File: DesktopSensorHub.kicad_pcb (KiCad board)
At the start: 2 copper layers, 44 parts, among them J1 USB_C_Receptacle_USB2.0, SW1 TS02-66-50-BK-160-LCR-D, U1 RP2040, U2 APDS-9960, U3 AP2112K-3.3, U5 W25Q32JVSS, Y1 12 MHZ

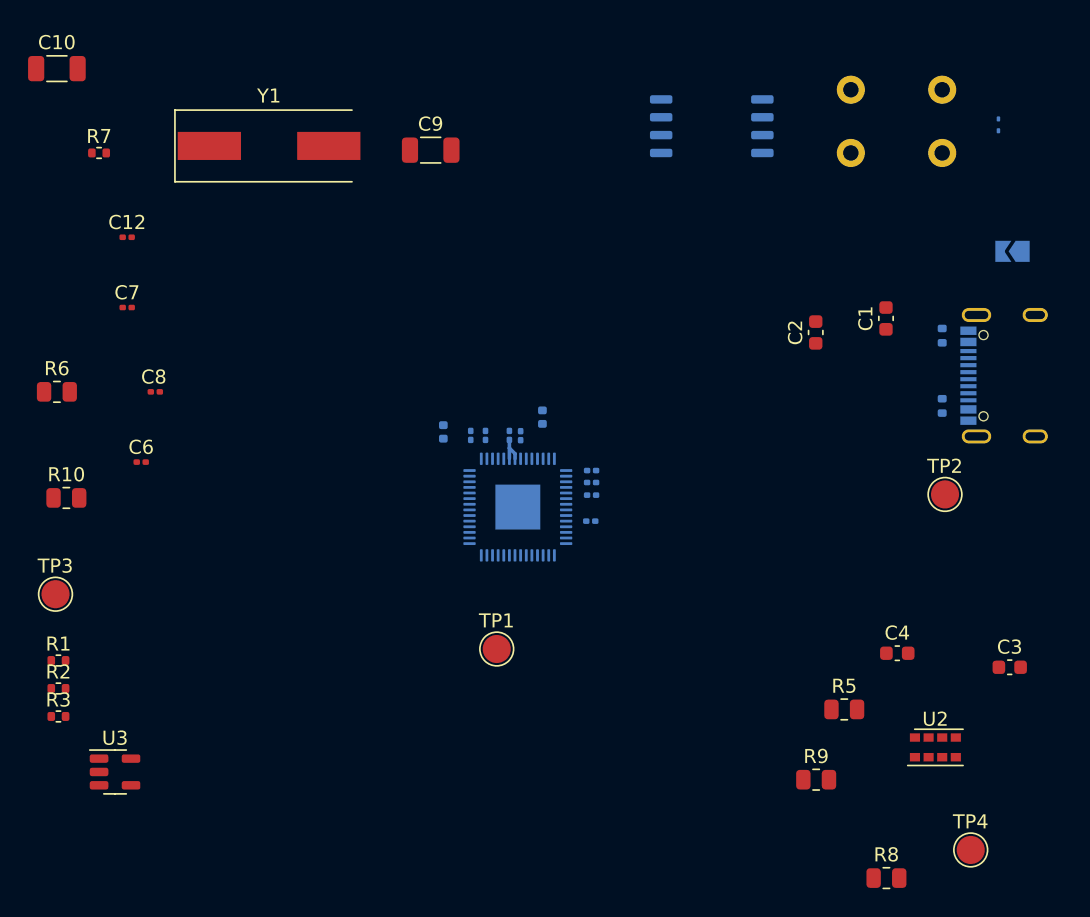
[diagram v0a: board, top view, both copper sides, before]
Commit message: finish layout, include design files sent to OSHPark
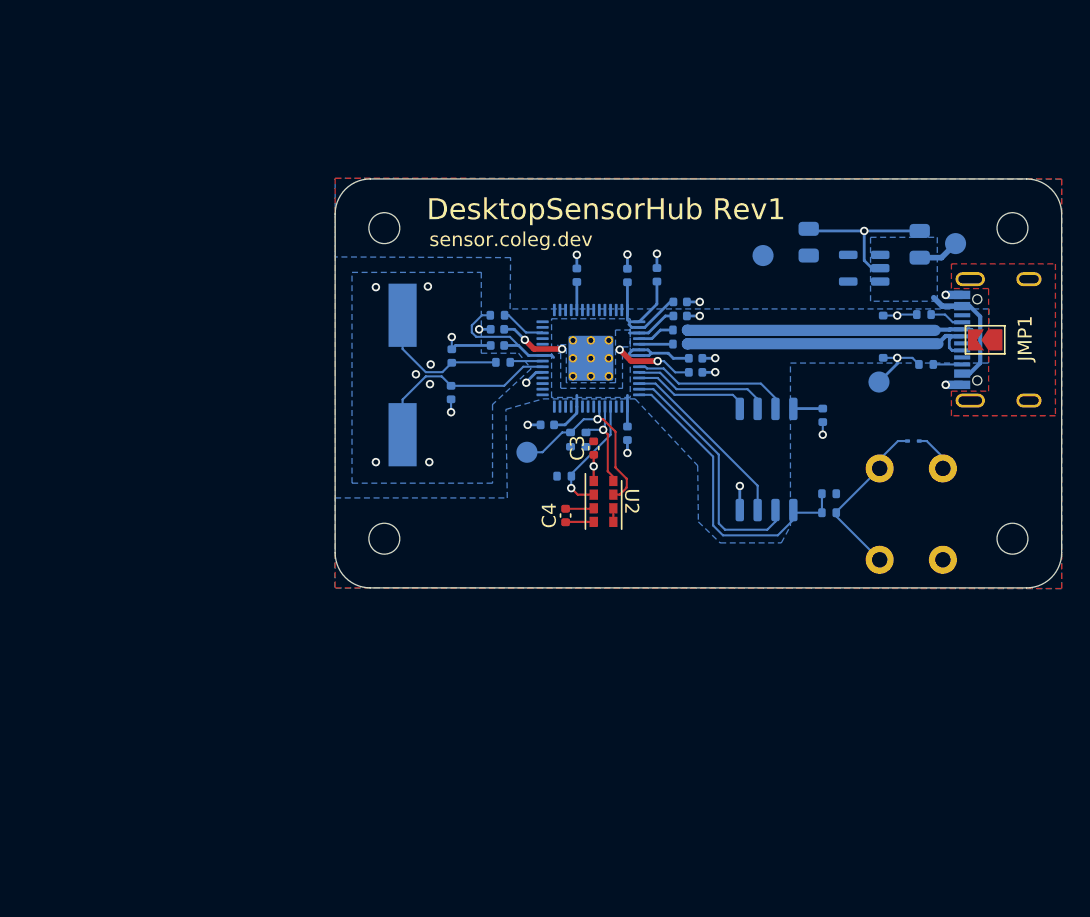
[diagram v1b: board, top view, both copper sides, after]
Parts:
- added REF**: MountingHole_2.2mm_M2, MountingHole:MountingHole_2.2mm_M2, F.Cu at (98.3, 88.5)
- added REF**: MountingHole_2.2mm_M2, MountingHole:MountingHole_2.2mm_M2, F.Cu at (143.0, 88.5)
- added REF**: MountingHole_2.2mm_M2, MountingHole:MountingHole_2.2mm_M2, F.Cu at (143.0, 66.3)
- added REF**: MountingHole_2.2mm_M2, MountingHole:MountingHole_2.2mm_M2, F.Cu at (98.3, 66.3)
- C1, C2: footprint Capacitor_SMD:C_0603_1608Metric -> Capacitor_SMD:C_0402_1005Metric; moved to B.Cu
- C10, C9: footprint Capacitor_SMD:C_1206_3216Metric -> Capacitor_SMD:C_0402_1005Metric; moved to B.Cu
- C12, C8: footprint Capacitor_SMD:C_0201_0603Metric -> Capacitor_SMD:C_0402_1005Metric; moved to B.Cu
- C13, C14, C15, C16, C17, C18, C19, C20: footprint Capacitor_SMD:C_0201_0603Metric -> Capacitor_SMD:C_0402_1005Metric
- C3, C4: footprint Capacitor_SMD:C_0603_1608Metric -> Capacitor_SMD:C_0402_1005Metric
- C6, C7: footprint Capacitor_SMD:C_0201_0603Metric -> Capacitor_SMD:C_0805_2012Metric; moved to B.Cu
- JMP1: moved to F.Cu
- R1, R2, R3, R7, U3, Y1: moved to B.Cu
- R10, R5, R6, R8, R9: footprint Resistor_SMD:R_0805_2012Metric -> Resistor_SMD:R_0402_1005Metric; moved to B.Cu
- TP1, TP2, TP3, TP4: footprint TestPoint:TestPoint_Pad_D2.0mm -> TestPoint:TestPoint_Pad_D1.5mm; moved to B.Cu
- U1: footprint Package_DFN_QFN:QFN-56-1EP_7x7mm_P0.4mm_EP3.2x3.2mm -> DesktopSensorHub footprints:RP2040-QFN-56
- moved TP3 68.7 mm to (138.9, 67.5), turned to 180 degrees
- moved U3 64.2 mm to (132.4, 69.2), turned to 180 degrees
- moved C6 57.5 mm to (136.4, 67.5), turned to 90 degrees
- moved R1 55.8 mm to (129.9, 86.6)
- moved R10 54.3 mm to (129.9, 85.2), turned to 180 degrees
- moved R3 51.6 mm to (119.3, 74.6), turned to 180 degrees
- moved R2 51.1 mm to (119.3, 73.6), turned to 180 degrees
- moved C7 48.7 mm to (128.5, 67.3), turned to 90 degrees
- moved C8 47.5 mm to (129.5, 79.7), turned to -90 degrees
- moved TP4 42.4 mm to (108.5, 82.3), turned to 180 degrees
- moved C12 41.6 mm to (120.5, 76.6)
- moved R8 37.8 mm to (112.7, 81.4), turned to 90 degrees
- moved C10 34.8 mm to (103.1, 75.5), turned to -90 degrees
- moved TP1 33.8 mm to (125.2, 68.3), turned to 180 degrees
- moved C3 33.5 mm to (113.2, 82.0), turned to 90 degrees
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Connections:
- C1 pad 1: Net-(C1-Pad1) -> /USB_D-
- C14 pad 1: +3.3V -> +3V3
- C15 pad 1: +3.3V -> +3V3
- C16 pad 1: +3.3V -> +3V3
- C17 pad 1: +3.3V -> +3V3
- C18 pad 1: +3.3V -> +3V3
- C19 pad 1: +3.3V -> +3V3
- C2 pad 1: Net-(C2-Pad1) -> /USB_D+
- C20 pad 1: +3.3V -> +3V3
- C21 pad 1: +3.3V -> +3V3
- J1 pad A6: Net-(C2-Pad1) -> /USB_D+
- J1 pad A7: Net-(C1-Pad1) -> /USB_D-
- J1 pad B6: Net-(C2-Pad1) -> /USB_D+
- J1 pad B7: Net-(C1-Pad1) -> /USB_D-
- R2 pad 1: Net-(C1-Pad1) -> /USB_D-
- R2 pad 2: /USB_D- -> Net-(U1-USB_DM)
- R3 pad 1: Net-(C2-Pad1) -> /USB_D+
- R3 pad 2: /USB_D+ -> Net-(U1-USB_DP)
- R5 pad 2: Net-(U1-GPIO18) -> Net-(U1-GPIO4)
- R8 pad 2: Net-(U1-GPIO17) -> Net-(U1-GPIO3)
- R9 pad 2: Net-(U1-GPIO16) -> Net-(U1-GPIO2)
- TP1 pad 1: Net-(U1-RUN) -> +3V3
- TP3 pad 1: Net-(D1-A1) -> Net-(U3-EN)
- TP4 pad 1: Net-(U1-GPIO18) -> Net-(U1-GPIO4)
- U1 pad 1: +3.3V -> +3V3
- U1 pad 10: +3.3V -> +3V3
- U1 pad 22: +3.3V -> +3V3
- U1 pad 27: Net-(U1-GPIO16) -> unconnected-(U1-GPIO16-Pad27)
- U1 pad 28: Net-(U1-GPIO17) -> unconnected-(U1-GPIO17-Pad28)
- U1 pad 29: Net-(U1-GPIO18) -> unconnected-(U1-GPIO18-Pad29)
- U1 pad 33: +3.3V -> +3V3
- U1 pad 4: unconnected-(U1-GPIO2-Pad4) -> Net-(U1-GPIO2)
- U1 pad 42: +3.3V -> +3V3
- U1 pad 43: +3.3V -> +3V3
- U1 pad 44: +3.3V -> +3V3
- U1 pad 46: /USB_D- -> Net-(U1-USB_DM)
- U1 pad 47: /USB_D+ -> Net-(U1-USB_DP)
- U1 pad 48: +3.3V -> +3V3
- U1 pad 49: +3.3V -> +3V3
- U1 pad 5: unconnected-(U1-GPIO3-Pad5) -> Net-(U1-GPIO3)
- U1 pad 6: unconnected-(U1-GPIO4-Pad6) -> Net-(U1-GPIO4)
- U2 pad 1: Net-(U1-GPIO17) -> Net-(U1-GPIO3)
- U2 pad 2: Net-(U1-GPIO18) -> Net-(U1-GPIO4)
- U2 pad 7: Net-(U1-GPIO16) -> Net-(U1-GPIO2)
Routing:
- net GND: track 0.00 -> 44.3 mm, vias 0 -> 27
- net +3V3: track 0.00 -> 38.2 mm, vias 0 -> 1
- net Net-(U1-QSPI_SS): track 0.00 -> 22.6 mm
- net /USB_D+: track 0.00 -> 22.4 mm
- net /USB_D-: track 0.00 -> 22.1 mm
- net Net-(U1-QSPI_SD1): track 0.00 -> 17.8 mm
- net +1V1: track 0.00 -> 16.8 mm, vias 0 -> 4
- net Net-(U1-GPIO4): track 0.00 -> 14.1 mm, vias 0 -> 1
- net Net-(U1-XIN): track 0.00 -> 14.0 mm
- net Net-(U1-QSPI_SD2): track 0.00 -> 13.2 mm
- net Net-(D1-A1): track 0.00 -> 12.2 mm
- net Net-(U3-EN): track 0.00 -> 11.7 mm
- net Net-(U1-QSPI_SD3): track 0.00 -> 11.4 mm
- net Net-(U1-QSPI_SCLK): track 0.00 -> 10.6 mm
- net Net-(C10-Pad2): track 0.00 -> 10.0 mm
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- added copper zone on B.Cu, net +1V1
- added copper zone on B.Cu, net +3V3
- added copper zone on B.Cu, net GND
- added copper zone on F.Cu, net GND
- added copper zone on F.Cu, net Net-(J1-SHIELD)
- added copper zone on B.Cu, net Net-(U3-EN)
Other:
- board outline added: 51.7 x 29.1 mm
- board text added: "DesktopSensorHub Rev1"
- board text added: "sensor.coleg.dev"
